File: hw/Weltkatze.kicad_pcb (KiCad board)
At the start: 6 copper layers, 58.1 x 58.1 mm, 57 parts, among them J1 USB_C_Receptacle_USB2.0_14P, J4 LED_OUT, J6 UART, SW2 SW_Push, SW3 SW_Push, U6 SPX3819M5-L-3-3, U7 BMP280, U8 LSM303C, U9 ESP32-C6-MINI-1/U, Y1 32.768k

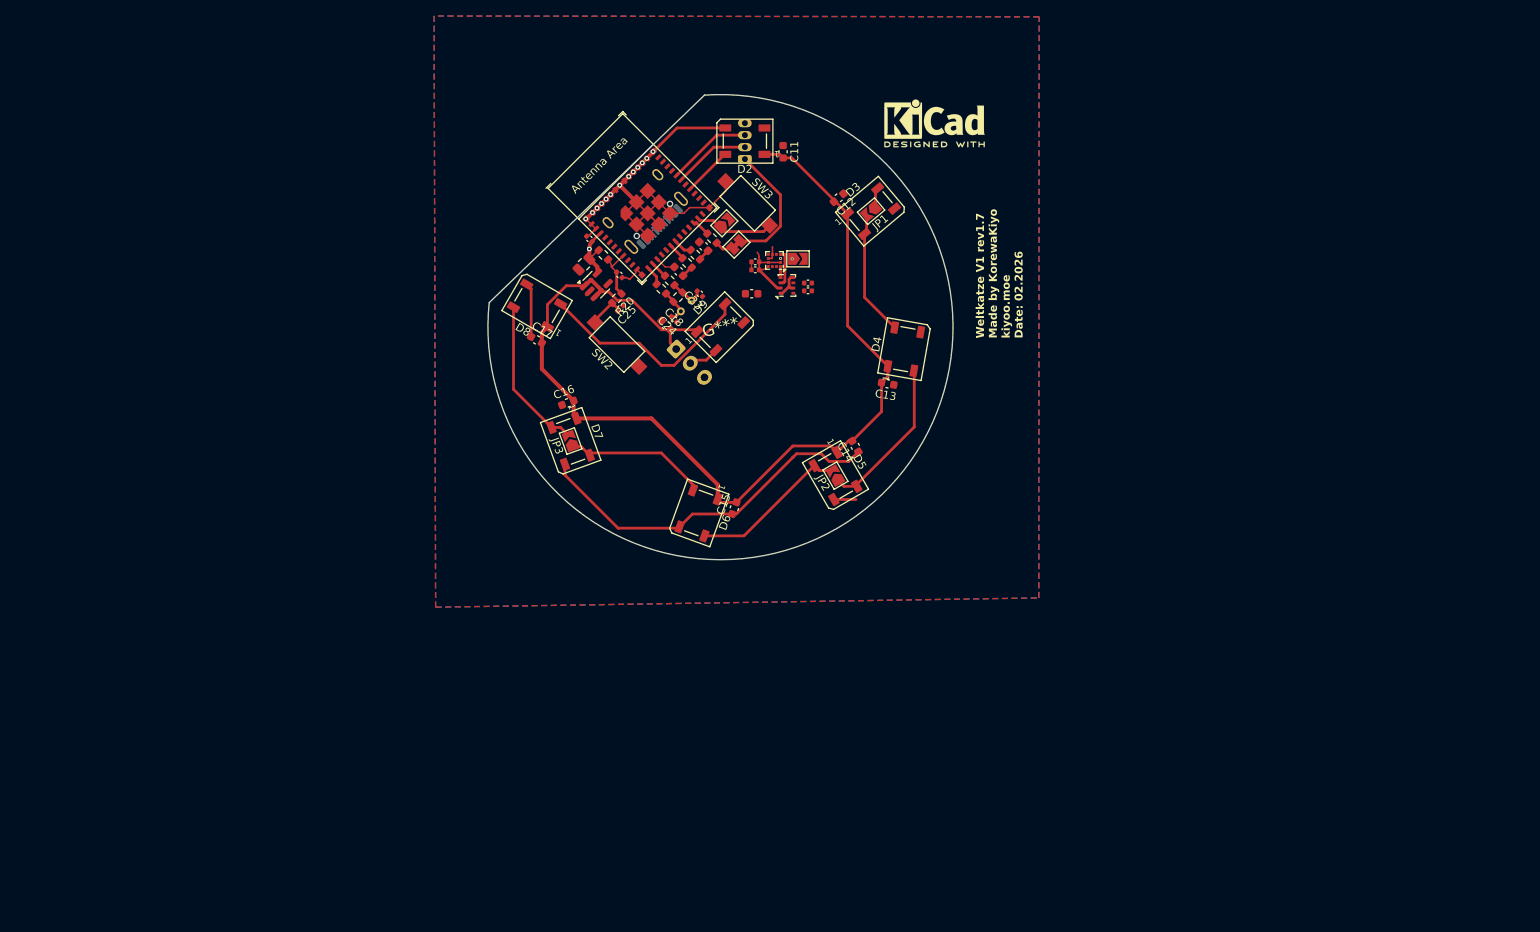
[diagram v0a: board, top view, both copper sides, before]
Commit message: USB fix and schematic cleanup (April work)
Add CR2 ESDA25P35 on the USB lines and tie VBUS straight to +5V, drop
the ESP_PWR header J7, JP9 and the VBAT_MON divider, add R25 4.7k and
wire the LSM303C I2C, remove the external LED output (D9, J4, C18).
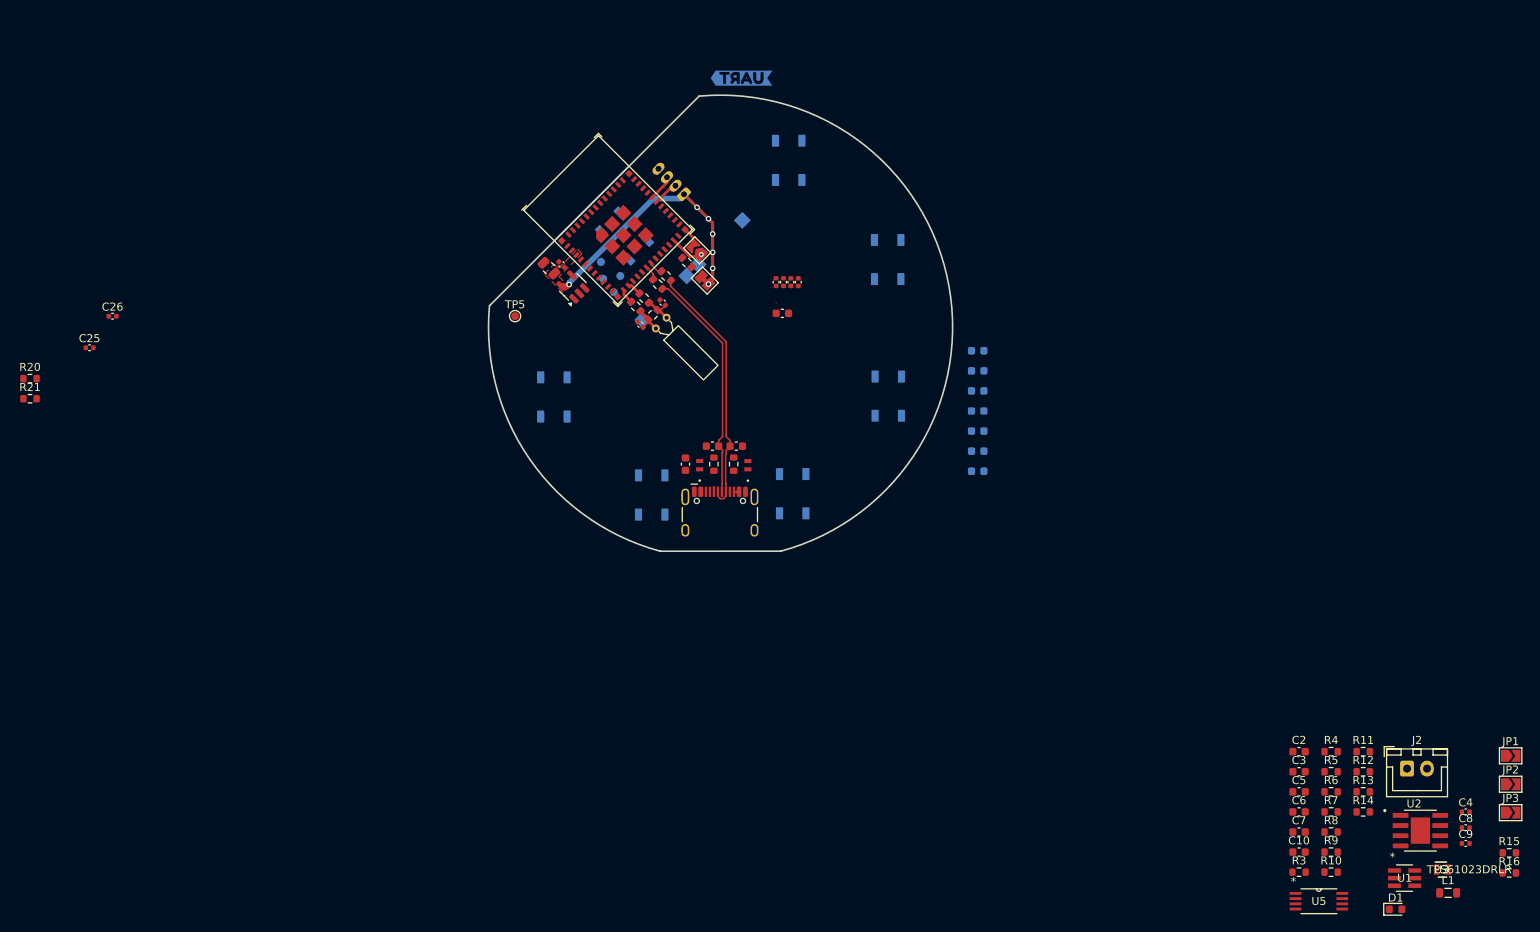
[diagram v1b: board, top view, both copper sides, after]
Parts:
- removed C18: 10u, Capacitor_SMD:C_0603_1608Metric
- removed D9: WS2812B, LED_SMD:LED_WS2812B_PLCC4_5.0x5.0mm_P3.2mm
- removed J4: LED_OUT, Connector_JST:JST_EH_B3B-EH-A_1x03_P2.50mm_Vertical
- removed JP9: SolderJumper_2_Open, Jumper:SolderJumper-2_P1.3mm_Open_TrianglePad1.0x1.5mm
- removed REF**: KiCad-Logo2_5mm_SilkScreen, Symbol:KiCad-Logo2_5mm_SilkScreen
- removed U7: BMP280, Package_LGA:Bosch_LGA-8_2x2.5mm_P0.65mm_ClockwisePinNumbering
- removed U8: LSM303C, Package_LGA:LGA-12_2x2mm_P0.5mm
- removed kibuzzard-67CB1547: G***, kibuzzard-67CB1547
- added C1: 10u, Capacitor_SMD:C_0603_1608Metric, F.Cu at (139.6, 109.1)
- added C10: 10u, Capacitor_SMD:C_0603_1608Metric, F.Cu at (216.3, 157.6)
- added C2: 10u, Capacitor_SMD:C_0603_1608Metric, F.Cu at (216.3, 145.1)
- added C3: 10u, Capacitor_SMD:C_0603_1608Metric, F.Cu at (216.3, 147.6)
- added C4: 0.1u, Capacitor_SMD:C_0402_1005Metric, F.Cu at (237.2, 152.6)
- added C5: 10u, Capacitor_SMD:C_0603_1608Metric, F.Cu at (216.3, 150.1)
- added C6: 10u, Capacitor_SMD:C_0603_1608Metric, F.Cu at (216.3, 152.6)
- added C7: 10u, Capacitor_SMD:C_0603_1608Metric, F.Cu at (216.3, 155.1)
- added C8: 0.1u, Capacitor_SMD:C_0402_1005Metric, F.Cu at (237.2, 154.6)
- added C9: 0.1u, Capacitor_SMD:C_0402_1005Metric, F.Cu at (237.2, 156.5)
- added CR1: ESDA25P35-1U1M, lib:QFN1610_STM-M, F.Cu at (147.4, 109.3)
- added CR2: ESDA25P35-1U1M, lib:QFN1610_STM-M, F.Cu at (141.4, 109.2)
- added D1: R, LED_SMD:LED_0603_1608Metric, F.Cu at (228.4, 164.8)
- added J2: CONN_BAT, Connector_JST:JST_XH_B2B-XH-A_1x02_P2.50mm_Vertical, F.Cu at (229.8, 147.2)
- added L1: 470n, Inductor_SMD:L_0805_2012Metric, F.Cu at (234.9, 162.7)
- added R1: 5.1k, Resistor_SMD:R_0603_1608Metric, F.Cu at (143.2, 109.1)
- added R10: 100k, Resistor_SMD:R_0603_1608Metric, F.Cu at (220.3, 160.1)
- added R11: 732k, Resistor_SMD:R_0603_1608Metric, F.Cu at (224.3, 145.1)
- added R12: 1k, Resistor_SMD:R_0603_1608Metric, F.Cu at (224.3, 147.6)
- added R13: 470, Resistor_SMD:R_0603_1608Metric, F.Cu at (224.3, 150.1)
- added R14: 191, Resistor_SMD:R_0603_1608Metric, F.Cu at (224.3, 152.6)
- added R15: 200k, Resistor_SMD:R_0603_1608Metric, F.Cu at (242.6, 157.7)
- added R16: 200k, Resistor_SMD:R_0603_1608Metric, F.Cu at (242.6, 160.2)
- added R2: 5.1k, Resistor_SMD:R_0603_1608Metric, F.Cu at (145.7, 109.1)
- added R3: 597k, Resistor_SMD:R_0603_1608Metric, F.Cu at (216.3, 160.1)
- added R4: 49.9k, Resistor_SMD:R_0603_1608Metric, F.Cu at (220.3, 145.1)
- added R5: 49.9k, Resistor_SMD:R_0603_1608Metric, F.Cu at (220.3, 147.6)
- added R6: 49.9k, Resistor_SMD:R_0603_1608Metric, F.Cu at (220.3, 150.1)
- added R7: 66.5k, Resistor_SMD:R_0603_1608Metric, F.Cu at (220.3, 152.6)
- added R8: 1k, Resistor_SMD:R_0603_1608Metric, F.Cu at (220.3, 155.1)
- added R9: 1.5k, Resistor_SMD:R_0603_1608Metric, F.Cu at (220.3, 157.6)
- added TP1: MTMS, TestPoint:TestPoint_Pad_D1.0mm, B.Cu at (129.1, 83.8)
- added TP2: MTDI, TestPoint:TestPoint_Pad_D1.0mm, B.Cu at (129.3, 86.0)
- added TP3: MTCK, TestPoint:TestPoint_Pad_D1.0mm, B.Cu at (130.7, 87.6)
- added TP4: MTDO, TestPoint:TestPoint_Pad_D1.0mm, B.Cu at (131.5, 85.6)
- added TP5: 3V3, TestPoint:TestPoint_Pad_D1.0mm, F.Cu at (118.3, 90.6)
- added U1: TPS3700DDCR, lib:DDC6_TEX-M, F.Cu at (229.5, 160.9)
- added U2: TP4056, lib:SOP127P600X175-9N, F.Cu at (231.5, 154.9)
- added U3: TPS61023DRLR, lib:DRL0006A, F.Cu at (234.2, 159.8)
- added U5: TPS2111APW, lib:PW8, F.Cu at (218.8, 163.8)
- added kibuzzard-698E3F4A: G***, kibuzzard-698E3F4A, B.Cu at (146.6, 60.9)
- C11, C12, C13, C14, C15, C16, C17, D2, D3, D4, D5, D6, D7, D8, SW2, SW3: moved to B.Cu
- J1, Y1: moved to F.Cu
- moved JP3 126.3 mm to (242.8, 152.7), turned to 0 degrees
- moved JP1 105.0 mm to (242.8, 145.6), turned to 0 degrees
- moved JP2 92.8 mm to (242.8, 149.1), turned to 0 degrees
- moved R20 74.0 mm to (57.7, 98.4), turned to 0 degrees
- moved R21 73.9 mm to (57.7, 100.9), turned to 0 degrees
- moved C25 66.5 mm to (65.1, 94.6), turned to 0 degrees
- moved C26 63.6 mm to (68.0, 90.6), turned to 0 degrees
- moved C17 55.2 mm to (176.2, 95.0), turned to 0 degrees
- moved C16 51.4 mm to (176.2, 97.5), turned to 0 degrees
- moved C11 46.8 mm to (176.2, 110.0), turned to 0 degrees
- moved J1 40.9 mm to (143.9, 116.3), turned to 0 degrees
- moved C12 36.1 mm to (176.2, 107.5), turned to 0 degrees
- moved C15 33.8 mm to (176.2, 100.0), turned to 0 degrees
- moved C29 25.3 mm to (146.0, 106.9), turned to 180 degrees
- moved C30 22.3 mm to (143.0, 106.9), turned to 0 degrees
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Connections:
- D8 pad 2: Net-(D8-DOUT) -> unconnected-(D8-DOUT-Pad2)
- J1 pad A4: /Power/USB_VBUS -> +5V
- J1 pad A9: /Power/USB_VBUS -> +5V
- J1 pad B4: /Power/USB_VBUS -> +5V
- J1 pad B9: /Power/USB_VBUS -> +5V
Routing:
- net +5V: track 132.5 -> 0.04 mm
- net GND: track 129.9 -> 2.75 mm, vias 13 -> 0
- net /Logic/USBD_P: track 1.52 -> 32.1 mm
- net /Logic/USBD_N: track 1.57 -> 30.0 mm
- net Net-(D8-DOUT): track 27.9 -> 0.00 mm
- net Net-(D4-DOUT): track 20.3 -> 0.00 mm
- net Net-(D5-DOUT): track 20.2 -> 0.00 mm
- net Net-(D7-DOUT): track 19.6 -> 0.00 mm
- net Net-(D6-DOUT): track 17.9 -> 0.00 mm
- net Net-(D3-DOUT): track 15.8 -> 0.00 mm
- net +3V3: track 33.5 -> 46.4 mm, vias 1 -> 7
- net /Logic/UART_TX: track 10.6 -> 3.27 mm
- net /Logic/ESP_RST: track 6.85 -> 0.00 mm
- net /Logic/UART_RX: track 9.68 -> 3.17 mm
- net /LEDs/LED_DIN: track 6.19 -> 0.00 mm
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- added copper zone on F.Cu, net +3V3
- removed copper zone on In1.Cu, net +5V
- removed copper zone on In3.Cu, net +5V
- removed copper zone on In4.Cu, net +5V
- removed copper zone on B.Cu, net GND
- removed copper zone on F.Cu, net GND
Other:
- board size 58.1 x 58.1 mm -> 58 x 57 mm
- copper layers 6 -> 2
- board text removed: "JLCJLCJLCJLC"
- board text removed: "Weltkatze V1 rev1.7 Made by KorewaKiyo kiyoo.moe Date: 02.2026"
